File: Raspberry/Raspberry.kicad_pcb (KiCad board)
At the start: 2 copper layers, 28 parts, among them J2 Conn_01x02, J3 Conn_01x03, J4 Conn_01x03, J5 Conn_01x03, J81 J8Header, J82 J8Header, Q1 BC337, Q2 BC337

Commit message: Korrekturen
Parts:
- added W3: Wire, RasperryLib:Wire_long, F.Cu at (189.2, 85.1)
- J4, J5: footprint RasperryLib:Conn_Small1x3 -> RasperryLib:Connector1x3
- moved 10k1 3.81 mm to (210.8, 85.1)
- moved W2 2.54 mm to (203.2, 90.2)
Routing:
- net Net-(F1-Pad1): track 110.5 -> 127.0 mm
- net Net-(10k1-Pad1): track 6.88 -> 13.2 mm
- net Net-(J4-Pad1): track 39.4 -> 34.3 mm
- net Net-(L1-Pad9): track 0.00 -> 3.81 mm
- net Net-(Bu1-Pad1): track 233.9 -> 236.4 mm
- net Net-(J4-Pad3): track 110.5 -> 107.9 mm
- net Net-(C1-Pad2): track 8.89 -> 11.4 mm
- net Net-(10k1-Pad2): track 248.9 -> 251.5 mm
- net Net-(C2-Pad2): track 8.89 -> 10.2 mm
- net Net-(J81-Pad28): track 63.9 -> 64.5 mm

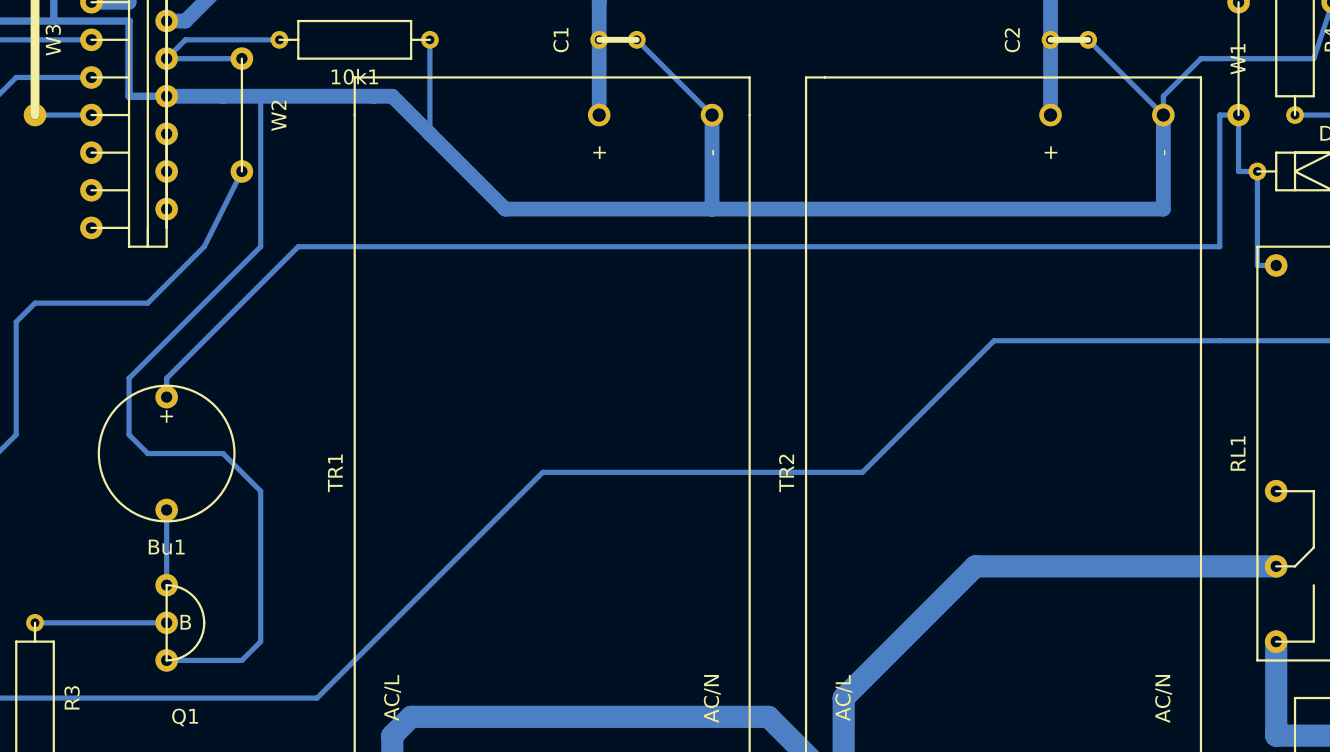
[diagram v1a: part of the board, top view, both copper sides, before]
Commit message: Buzzer 5v
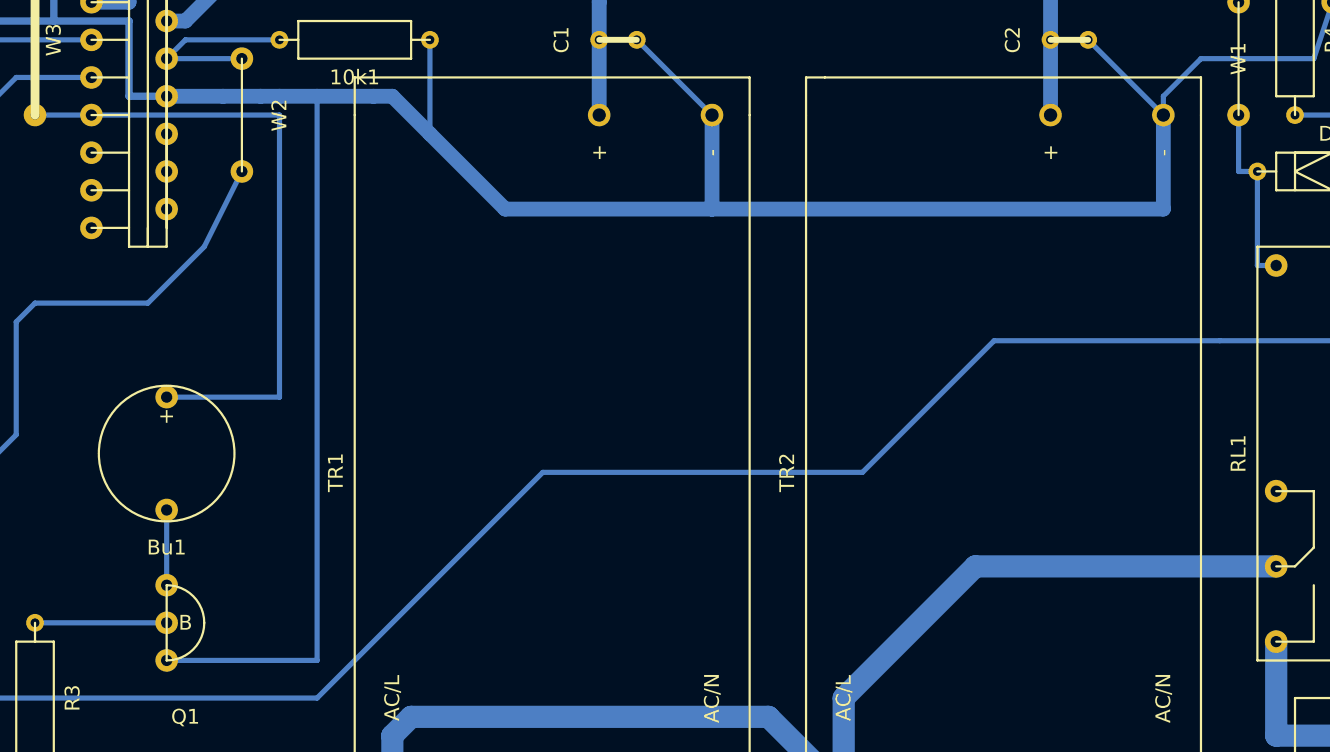
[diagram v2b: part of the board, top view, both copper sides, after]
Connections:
- D3 pad 2: Net-(Bu1-Pad1) -> Net-(D3-Pad2)
- D4 pad 2: Net-(Bu1-Pad1) -> Net-(D3-Pad2)
- D5 pad 2: Net-(Bu1-Pad1) -> Net-(D3-Pad2)
- F2 pad 1: Net-(Bu1-Pad1) -> Net-(D3-Pad2)
- L1 pad 4: Net-(Bu1-Pad1) -> Net-(D3-Pad2)
- L1 pad 9: Net-(L1-Pad9) -> Net-(Bu1-Pad1)
- RL1 pad 2: Net-(Bu1-Pad1) -> Net-(D3-Pad2)
- W1 pad 1: Net-(Bu1-Pad1) -> Net-(D3-Pad2)
- W1 pad 2: Net-(Bu1-Pad1) -> Net-(D3-Pad2)
- W3 pad 1: Net-(L1-Pad9) -> Net-(Bu1-Pad1)
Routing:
- net Net-(Bu1-Pad1): track 236.4 -> 43.2 mm
- net Net-(D3-Pad2): track 0.00 -> 150.2 mm
- net Net-(10k1-Pad2): track 251.5 -> 245.7 mm
- net Net-(L1-Pad9): track 3.81 -> 0.00 mm
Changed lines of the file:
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@@
     (thickness 1.6)
     (drawings 7)
-    (tracks 325)
+    (tracks 317)
     (zones 0)
     (modules 29)
@@
   (net 63 "Net-(J81-Pad28)")
   (net 64 "Net-(J81-Pad20)")
-  (net 65 "Net-(L1-Pad9)")
+  (net 65 "Net-(D3-Pad2)")
   (net_class Default "Dies ist die voreingestellte Netzklasse."
     (clearance 0.2)
@@
     (add_net "Net-(D1-Pad2)")
     (add_net "Net-(D2-Pad2)")
+    (add_net "Net-(D3-Pad2)")
     (add_net "Net-(D5-Pad1)")
     (add_net "Net-(F1-Pad1)")
@@
     (add_net "Net-(L1-Pad14)")
     (add_net "Net-(L1-Pad15)")
-    (add_net "Net-(L1-Pad9)")
     (add_net "Net-(Q1-Pad2)")
     (add_net "Net-(Q2-Pad2)")
@@
       (net 7 "Net-(D1-Pad2)"))
     (pad 2 thru_hole circle (at 5.08 0) (size 1.2 1.2) (drill 0.6) (layers *.Cu *.Mask)
-      (net 3 "Net-(Bu1-Pad1)"))
+      (net 65 "Net-(D3-Pad2)"))
   )
   (module RasperryLib:Diode (layer F.Cu)
@@
       (net 8 "Net-(D2-Pad2)"))
     (pad 2 thru_hole circle (at 5.08 0) (size 1.2 1.2) (drill 0.6) (layers *.Cu *.Mask)
-      (net 3 "Net-(Bu1-Pad1)"))
+      (net 65 "Net-(D3-Pad2)"))
   )
   (module RasperryLib:Diode (layer F.Cu)
@@
       (net 9 "Net-(D5-Pad1)"))
     (pad 2 thru_hole circle (at 5.08 0 180) (size 1.2 1.2) (drill 0.6) (layers *.Cu *.Mask)
-      (net 3 "Net-(Bu1-Pad1)"))
+      (net 65 "Net-(D3-Pad2)"))
   )
   (module RasperryLib:Conn_Small1x2 (layer F.Cu)
@@
       (net 7 "Net-(D1-Pad2)"))
     (pad 4 thru_hole circle (at -2.54 3.81 180) (size 1.524 1.524) (drill 0.762) (layers *.Cu *.Mask)
-      (net 3 "Net-(Bu1-Pad1)"))
+      (net 65 "Net-(D3-Pad2)"))
     (pad 5 thru_hole circle (at 2.54 2.54 180) (size 1.524 1.524) (drill 0.762) (layers *.Cu *.Mask)
       (net 20 "Net-(J81-Pad8)"))
@@
       (net 2 "Net-(10k1-Pad2)"))
     (pad 9 thru_hole circle (at 2.54 -2.54 180) (size 1.524 1.524) (drill 0.762) (layers *.Cu *.Mask)
-      (net 65 "Net-(L1-Pad9)"))
+      (net 3 "Net-(Bu1-Pad1)"))
     (pad 10 thru_hole circle (at -2.54 -3.81 180) (size 1.524 1.524) (drill 0.762) (layers *.Cu *.Mask)
       (net 50 "Net-(L1-Pad10)"))
@@
       (net 9 "Net-(D5-Pad1)"))
     (pad 2 thru_hole circle (at -12.7 3.81 270) (size 1.524 1.524) (drill 0.762) (layers *.Cu *.Mask)
-      (net 3 "Net-(Bu1-Pad1)"))
+      (net 65 "Net-(D3-Pad2)"))
     (pad 3 thru_hole circle (at 2.54 3.81 270) (size 1.524 1.524) (drill 0.762) (layers *.Cu *.Mask)
       (net 58 "Net-(RL1-Pad3)"))
@@
     (fp_line (start -3.81 0) (end 3.81 0) (layer F.SilkS) (width 0.15))
     (pad 1 thru_hole circle (at -3.81 0 270) (size 1.524 1.524) (drill 0.762) (layers *.Cu *.Mask)
-      (net 3 "Net-(Bu1-Pad1)"))
+      (net 65 "Net-(D3-Pad2)"))
     (pad 2 thru_hole circle (at 3.81 0 270) (size 1.524 1.524) (drill 0.762) (layers *.Cu *.Mask)
-      (net 3 "Net-(Bu1-Pad1)"))
+      (net 65 "Net-(D3-Pad2)"))
   )
   (module RasperryLib:Wire_Short (layer F.Cu)
@@
       (net 62 "Net-(F1-Pad1)"))
     (pad 1 thru_hole circle (at -5.08 0 90) (size 1.524 1.524) (drill 0.6) (layers *.Cu *.Mask)
-      (net 65 "Net-(L1-Pad9)"))
+      (net 3 "Net-(Bu1-Pad1)"))
   )
   (module RasperryLib:Fuse (layer F.Cu)
@@
     (fp_line (start -11.43 5.08) (end 11.43 5.08) (layer F.SilkS) (width 0.15))
     (pad 1 thru_hole circle (at 11.43 0 90) (size 1.2 1.2) (drill 0.8) (layers *.Cu *.Mask)
-      (net 3 "Net-(Bu1-Pad1)"))
+      (net 65 "Net-(D3-Pad2)"))
     (pad 2 thru_hole circle (at -11.43 0 90) (size 1.2 1.2) (drill 0.8) (layers *.Cu *.Mask)
       (net 6 "Net-(C2-Pad2)"))
@@
   (segment (start 199.39 85.09) (end 198.12 86.36) (width 0.35) (layer B.Cu) (net 1))
   (segment (start 205.74 85.09) (end 199.39 85.09) (width 0.35) (layer B.Cu) (net 1) (status 10))
+  (segment (start 208.28 88.9) (end 208.28 127) (width 0.35) (layer B.Cu) (net 2))
+  (segment (start 208.28 127) (end 198.12 127) (width 0.35) (layer B.Cu) (net 2))
   (segment (start 215.9 85.09) (end 215.9 91.44) (width 0.35) (layer B.Cu) (net 2))
-  (segment (start 204.47 88.9) (end 204.47 99.06) (width 0.35) (layer B.Cu) (net 2))
-  (segment (start 203.2 127) (end 198.12 127) (width 0.35) (layer B.Cu) (net 2))
-  (segment (start 204.47 125.73) (end 203.2 127) (width 0.35) (layer B.Cu) (net 2))
-  (segment (start 204.47 115.57) (end 204.47 125.73) (width 0.35) (layer B.Cu) (net 2))
-  (segment (start 201.93 113.03) (end 204.47 115.57) (width 0.35) (layer B.Cu) (net 2))
-  (segment (start 196.85 113.03) (end 201.93 113.03) (width 0.35) (layer B.Cu) (net 2))
-  (segment (start 195.58 111.76) (end 196.85 113.03) (width 0.35) (layer B.Cu) (net 2))
-  (segment (start 195.58 107.95) (end 195.58 111.76) (width 0.35) (layer B.Cu) (net 2))
-  (segment (start 204.47 99.06) (end 195.58 107.95) (width 0.35) (layer B.Cu) (net 2))
   (segment (start 190.5 83.82) (end 190.5 80.01) (width 0.5) (layer B.Cu) (net 2))
   (segment (start 198.12 88.9) (end 195.58 88.9) (width 0.5) (layer B.Cu) (net 2))
@@
   (segment (start 215.9 91.44) (end 213.36 88.9) (width 1) (layer B.Cu) (net 2))
   (segment (start 234.95 96.52) (end 220.98 96.52) (width 1) (layer B.Cu) (net 2))
-  (segment (start 212.09 88.9) (end 205.74 88.9) (width 1) (layer B.Cu) (net 2))
+  (segment (start 212.09 88.9) (end 208.28 88.9) (width 1) (layer B.Cu) (net 2))
+  (segment (start 208.28 88.9) (end 205.74 88.9) (width 1) (layer B.Cu) (net 2))
   (segment (start 205.74 88.9) (end 204.47 88.9) (width 1) (layer B.Cu) (net 2))
   (segment (start 204.47 88.9) (end 201.93 88.9) (width 1) (layer B.Cu) (net 2))
@@
   (segment (start 191.339 80.01) (end 193.04 80.01) (width 0.35) (layer B.Cu) (net 2))
   (segment (start 190.5 73.66) (end 190.5 80.01) (width 0.35) (layer B.Cu) (net 2))
-  (segment (start 257.81 54.61) (end 257.81 57.15) (width 0.8) (layer B.Cu) (net 3))
-  (segment (start 198.12 109.22) (end 198.12 107.95) (width 0.35) (layer B.Cu) (net 3))
-  (segment (start 269.24 90.17) (end 270.51 90.17) (width 0.35) (layer B.Cu) (net 3))
-  (segment (start 269.24 99.06) (end 269.24 90.17) (width 0.35) (layer B.Cu) (net 3))
-  (segment (start 207.01 99.06) (end 269.24 99.06) (width 0.35) (layer B.Cu) (net 3))
-  (segment (start 198.12 107.95) (end 207.01 99.06) (width 0.35) (layer B.Cu) (net 3))
-  (segment (start 215.9 73.66) (end 215.9 80.01) (width 1) (layer B.Cu) (net 3))
-  (segment (start 199.39 83.82) (end 198.12 83.82) (width 1) (layer B.Cu) (net 3))
-  (segment (start 203.2 80.01) (end 199.39 83.82) (width 1) (layer B.Cu) (net 3))
-  (segment (start 215.9 80.01) (end 203.2 80.01) (width 1) (layer B.Cu) (net 3))
-  (segment (start 215.9 67.31) (end 215.9 73.66) (width 1) (layer B.Cu) (net 3))
-  (segment (start 257.81 54.61) (end 243.84 54.61) (width 1) (layer B.Cu) (net 3))
-  (segment (start 243.84 67.31) (end 215.9 67.31) (width 1) (layer B.Cu) (net 3))
-  (segment (start 215.9 67.31) (end 209.55 67.31) (width 1) (layer B.Cu) (net 3))
-  (segment (start 243.84 54.61) (end 243.84 67.31) (width 1) (layer B.Cu) (net 3))
-  (segment (start 257.81 55.88) (end 257.81 54.61) (width 0.35) (layer B.Cu) (net 3))
-  (segment (start 270.51 54.61) (end 270.51 82.55) (width 0.35) (layer B.Cu) (net 3))
-  (segment (start 257.81 54.61) (end 270.51 54.61) (width 0.35) (layer B.Cu) (net 3))
-  (segment (start 271.78 93.98) (end 271.78 100.33) (width 0.35) (layer B.Cu) (net 3))
-  (segment (start 271.78 100.33) (end 273.05 100.33) (width 0.35) (layer B.Cu) (net 3))
-  (segment (start 270.51 90.17) (end 270.51 93.98) (width 0.35) (layer B.Cu) (net 3))
-  (segment (start 270.51 93.98) (end 271.78 93.98) (width 0.35) (layer B.Cu) (net 3))
+  (segment (start 193.04 90.17) (end 205.74 90.17) (width 0.35) (layer B.Cu) (net 3) (status 400000))
+  (segment (start 205.74 109.22) (end 198.12 109.22) (width 0.35) (layer B.Cu) (net 3) (status 800000))
+  (segment (start 205.74 90.17) (end 205.74 109.22) (width 0.35) (layer B.Cu) (net 3))
+  (segment (start 189.23 90.17) (end 193.04 90.17) (width 0.35) (layer B.Cu) (net 3))
   (segment (start 198.12 121.92) (end 198.12 116.84) (width 0.35) (layer B.Cu) (net 4))
   (segment (start 227.33 82.55) (end 227.33 80.01) (width 0.8) (layer B.Cu) (net 5))
@@
   (segment (start 170.18 102.87) (end 172.72 102.87) (width 0.35) (layer B.Cu) (net 64))
   (segment (start 168.91 104.14) (end 170.18 102.87) (width 0.35) (layer B.Cu) (net 64))
-  (segment (start 189.23 90.17) (end 193.04 90.17) (width 0.35) (layer B.Cu) (net 65))
+  (segment (start 257.81 54.61) (end 257.81 57.15) (width 0.8) (layer B.Cu) (net 65))
+  (segment (start 215.9 73.66) (end 215.9 80.01) (width 1) (layer B.Cu) (net 65))
+  (segment (start 199.39 83.82) (end 198.12 83.82) (width 1) (layer B.Cu) (net 65))
+  (segment (start 203.2 80.01) (end 199.39 83.82) (width 1) (layer B.Cu) (net 65))
+  (segment (start 215.9 80.01) (end 203.2 80.01) (width 1) (layer B.Cu) (net 65))
+  (segment (start 215.9 67.31) (end 215.9 73.66) (width 1) (layer B.Cu) (net 65))
+  (segment (start 257.81 54.61) (end 243.84 54.61) (width 1) (layer B.Cu) (net 65))
+  (segment (start 243.84 67.31) (end 215.9 67.31) (width 1) (layer B.Cu) (net 65))
+  (segment (start 215.9 67.31) (end 209.55 67.31) (width 1) (layer B.Cu) (net 65))
+  (segment (start 243.84 54.61) (end 243.84 67.31) (width 1) (layer B.Cu) (net 65))
+  (segment (start 257.81 55.88) (end 257.81 54.61) (width 0.35) (layer B.Cu) (net 65))
+  (segment (start 270.51 54.61) (end 270.51 82.55) (width 0.35) (layer B.Cu) (net 65))
+  (segment (start 257.81 54.61) (end 270.51 54.61) (width 0.35) (layer B.Cu) (net 65))
+  (segment (start 271.78 93.98) (end 271.78 100.33) (width 0.35) (layer B.Cu) (net 65))
+  (segment (start 271.78 100.33) (end 273.05 100.33) (width 0.35) (layer B.Cu) (net 65))
+  (segment (start 270.51 90.17) (end 270.51 93.98) (width 0.35) (layer B.Cu) (net 65))
+  (segment (start 270.51 93.98) (end 271.78 93.98) (width 0.35) (layer B.Cu) (net 65))
 )

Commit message: second design with turned header
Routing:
- net Net-(D3-Pad2): track 150.2 -> 148.9 mm
- net Net-(C1-Pad2): track 11.4 -> 10.2 mm
